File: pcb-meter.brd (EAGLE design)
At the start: 65.5 x 35 mm, 47 parts

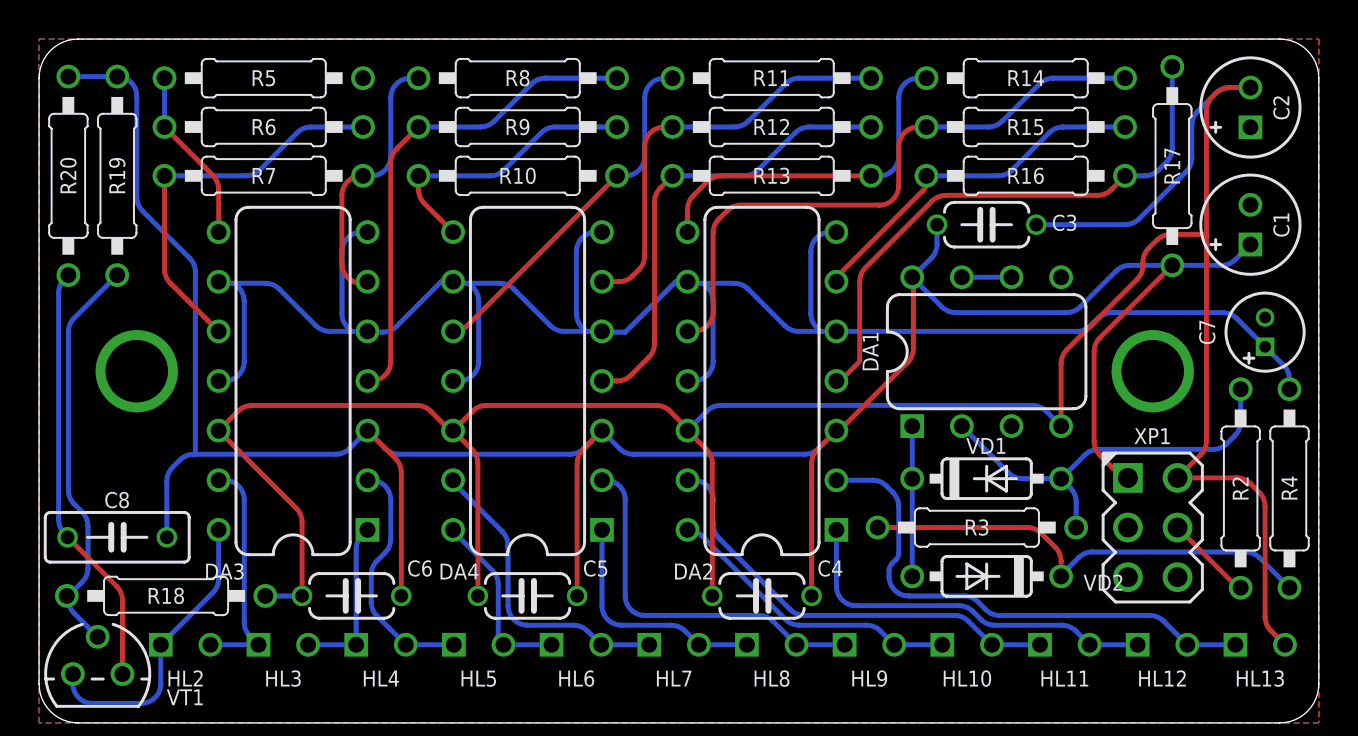
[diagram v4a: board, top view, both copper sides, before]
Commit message: Add Meter Board
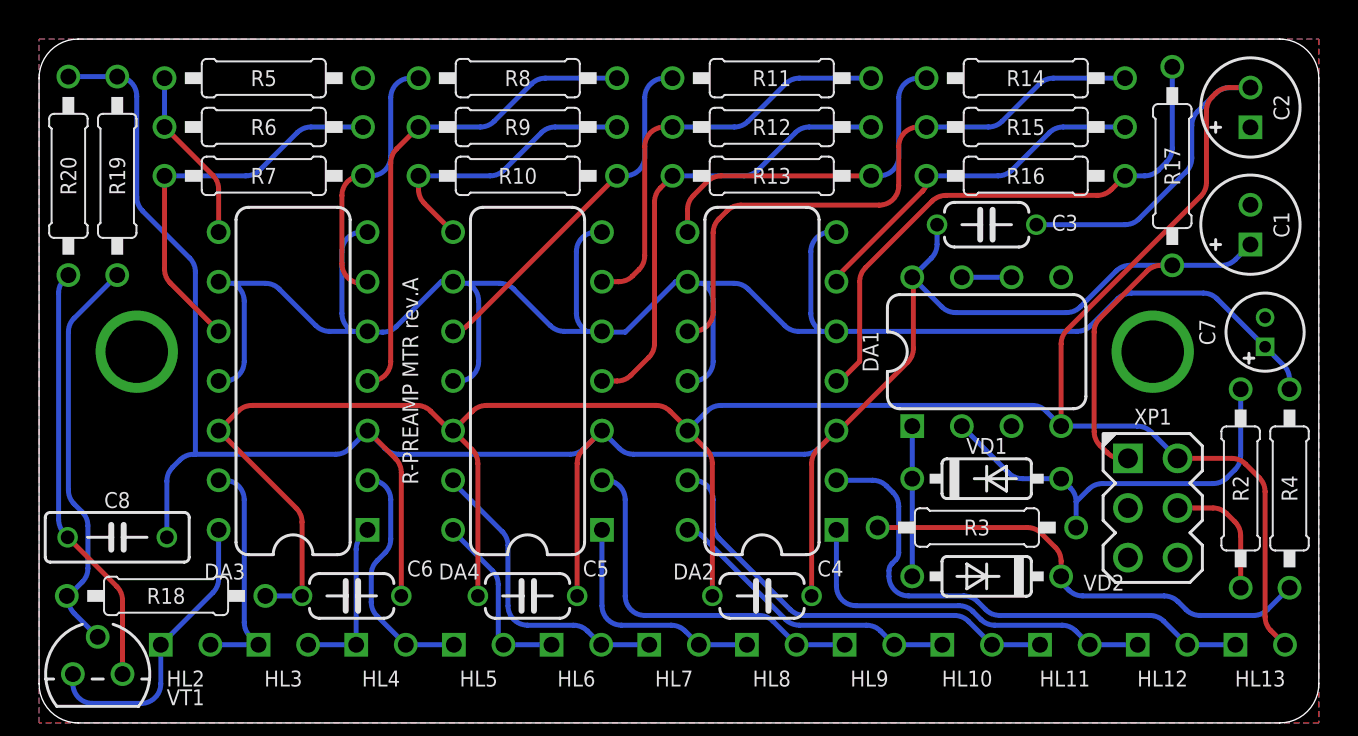
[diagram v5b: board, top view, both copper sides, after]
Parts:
- added PCB1: R-PREAMP MTR rev.A, module-footprints:F-LOGO
- C1, C2: value 10u/35V -> 10U/35V
- C3, C4, C5, C6: value 100n -> 100N(TH)
- C7: value 1u/50V -> 1U/50V
- C8: value 47n -> 47N(FILM)
- R10: value 560R -> 560R(TH)
- R11: value 820R -> 820R(TH)
- R12: value 1.2k -> 1K2(TH)
- R13: value 1.5k -> 1K5(TH)
- R14: value 2.2k -> 2K2(TH)
- R15: value 3.3k -> 3K3(TH)
- R16: value 12k -> 12K(TH)
- R17: value 5.6k -> 5K6(TH)
- R18: value 15k -> 15K(TH)
- R19: value 1k -> 1K(TH)
- R2: value 56k -> 56K(TH)
- R20: value 180R -> 180R(TH)
- R3: value 150k -> 150K(TH)
- R4: value 1.8k -> 1K8(TH)
- R5: value 270R -> 270R(TH)
- R6, R7: value 220R -> 220R(TH)
- R8, R9: value 330R -> 330R(TH)
- moved XP1 1.00 mm to (90.0, 13.0)
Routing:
- net -15V: track 139.7 -> 132.9 mm
- net N$2: track 4.51 -> 6.60 mm
- net N$26: track 97.5 -> 98.3 mm
- net N$5: track 21.0 -> 21.7 mm

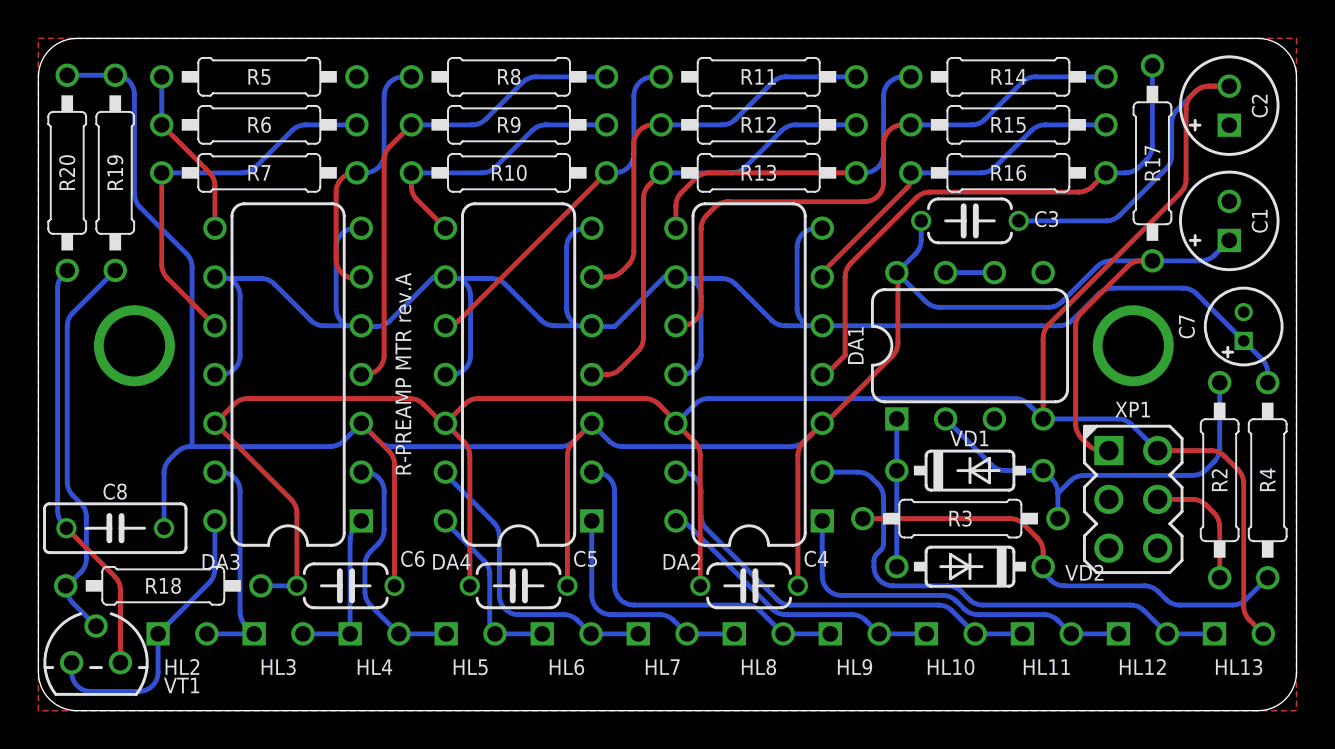
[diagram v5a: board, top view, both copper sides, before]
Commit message: Change meter PCB size
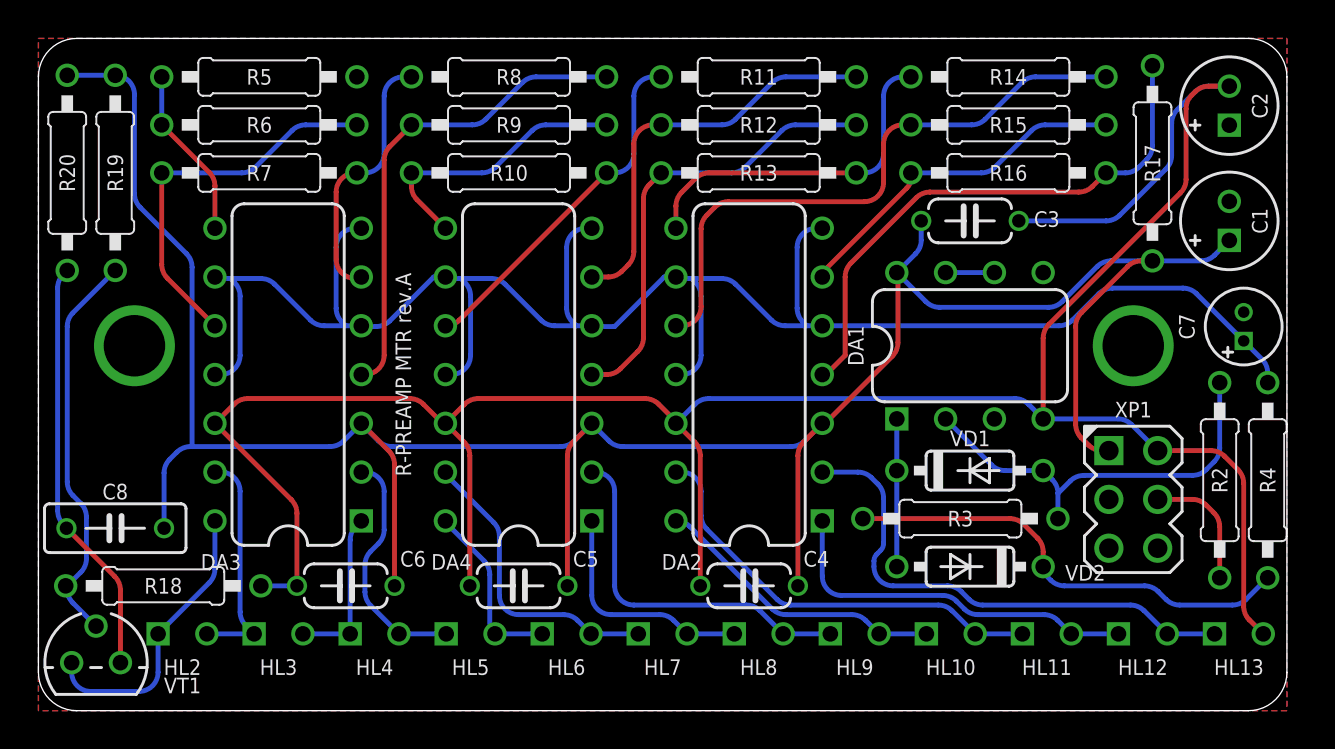
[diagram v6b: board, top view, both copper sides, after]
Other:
- board size 65.5 x 35 mm -> 65 x 35 mm
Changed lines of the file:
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@@
 <wire x1="33" y1="35" x2="33" y2="4" width="0" layer="20"/>
 <wire x1="33" y1="4" x2="35" y2="2" width="0" layer="20" curve="90"/>
-<wire x1="35" y1="2" x2="96.5" y2="2" width="0" layer="20"/>
-<wire x1="96.5" y1="2" x2="98.5" y2="4" width="0" layer="20" curve="90"/>
-<wire x1="98.5" y1="4" x2="98.5" y2="35" width="0" layer="20"/>
-<wire x1="98.5" y1="35" x2="96.5" y2="37" width="0" layer="20" curve="90"/>
-<wire x1="96.5" y1="37" x2="35" y2="37" width="0" layer="20"/>
+<wire x1="35" y1="2" x2="96" y2="2" width="0" layer="20"/>
+<wire x1="96" y1="2" x2="98" y2="4" width="0" layer="20" curve="90"/>
+<wire x1="98" y1="4" x2="98" y2="35" width="0" layer="20"/>
+<wire x1="98" y1="35" x2="96" y2="37" width="0" layer="20" curve="90"/>
+<wire x1="96" y1="37" x2="35" y2="37" width="0" layer="20"/>
 <wire x1="35" y1="37" x2="33" y2="35" width="0" layer="20" curve="90"/>
 </plain>
@@
 <polygon width="0.254" layer="16">
 <vertex x="33" y="37"/>
-<vertex x="98.5" y="37"/>
-<vertex x="98.5" y="2"/>
+<vertex x="98" y="37"/>
+<vertex x="98" y="2"/>
 <vertex x="33" y="2"/>
 </polygon>
 <polygon width="0.254" layer="1">
 <vertex x="33" y="37"/>
-<vertex x="98.5" y="37"/>
-<vertex x="98.5" y="2"/>
+<vertex x="98" y="37"/>
+<vertex x="98" y="2"/>
 <vertex x="33" y="2"/>
 </polygon>

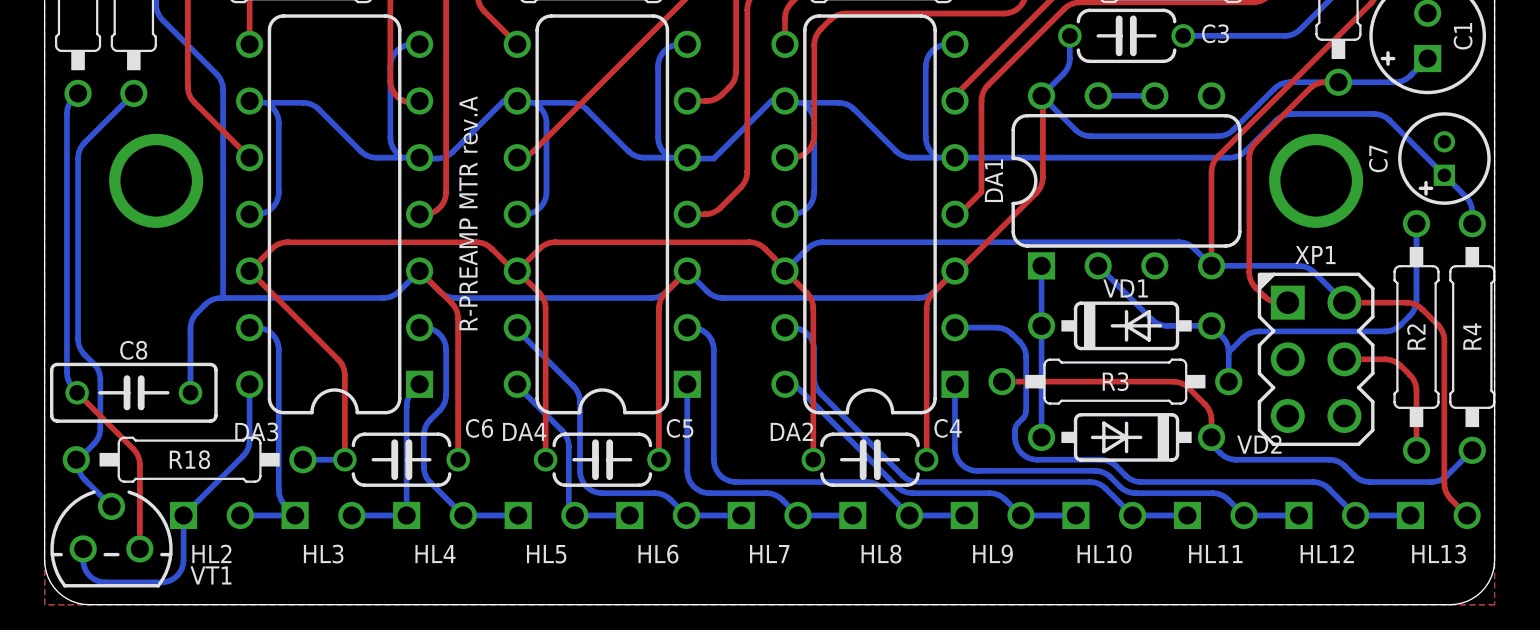
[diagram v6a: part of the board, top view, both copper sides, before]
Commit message: Change LED/front panel spacing
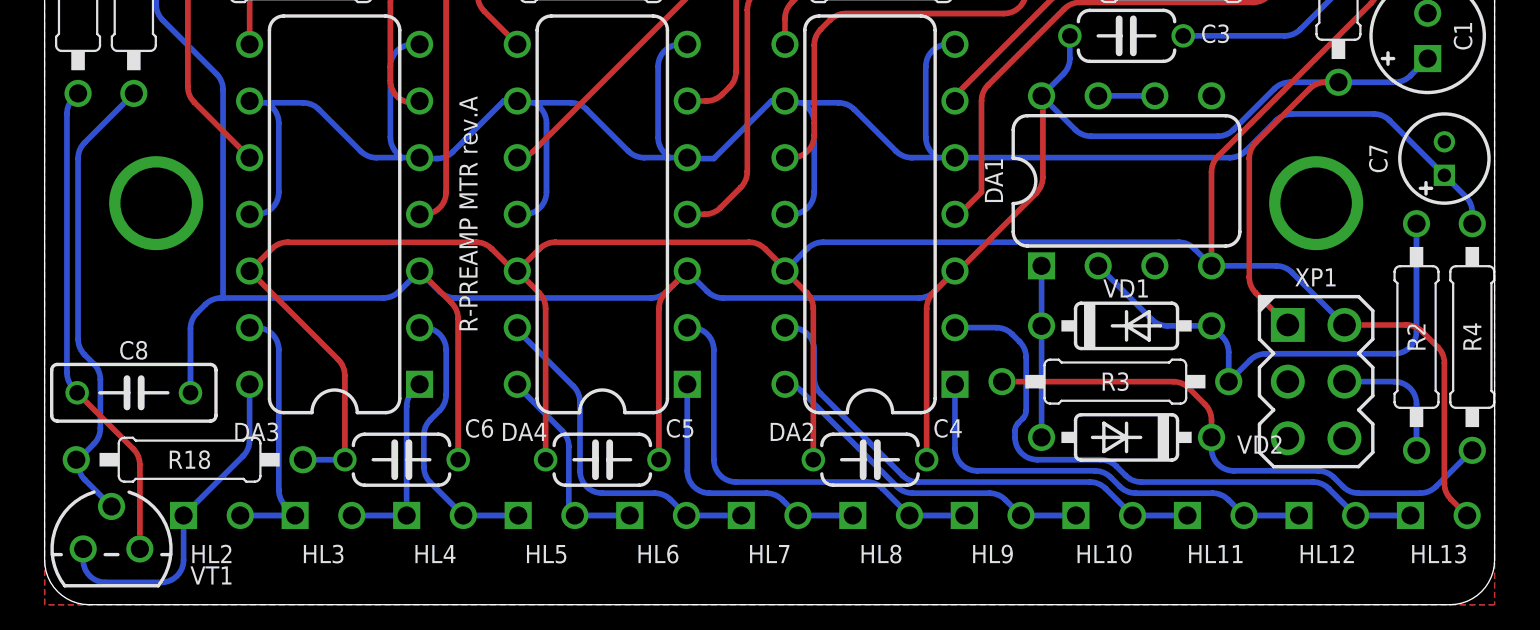
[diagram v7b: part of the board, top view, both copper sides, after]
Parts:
- moved XP1 1.00 mm to (90.0, 12.0)
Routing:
- net N$5: track 21.7 -> 23.0 mm
- net N$2: track 6.60 -> 5.72 mm
- net +15V: track 135.3 -> 136.0 mm
- net N$8: track 24.0 -> 24.6 mm
- net -15V: track 132.9 -> 132.3 mm
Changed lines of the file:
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@@
 </autorouter>
 <elements>
-<element name="XP1" library="connectors" package="MA03-2" value="" x="90" y="13" rot="R270"/>
+<element name="XP1" library="connectors" package="MA03-2" value="" x="90" y="12" rot="R270"/>
 <element name="R2" library="resistors" package="R-0207/10" value="56K(TH)" x="94.5" y="14" rot="R90"/>
 <element name="DA1" library="ic-ti" package="DIP-8" value="TL072IP" x="81.5" y="21">
@@
 <wire x1="92.45710625" y1="28.95710625" x2="85.60289375" y2="22.10289375" width="0.254" layer="1"/>
 <wire x1="85.60289375" y1="22.10289375" x2="85.31" y2="21.3957875" width="0.254" layer="1" curve="45"/>
-<wire x1="91.27" y1="15.54" x2="94.0457875" y2="15.54" width="0.254" layer="1"/>
-<wire x1="94.0457875" y1="15.54" x2="94.75289375" y2="15.24710625" width="0.254" layer="1" curve="-45"/>
-<wire x1="94.75289375" y1="15.24710625" x2="95.45710625" y2="14.54289375" width="0.254" layer="1"/>
-<wire x1="95.45710625" y1="14.54289375" x2="95.75" y2="13.8357875" width="0.254" layer="1" curve="-45"/>
-<wire x1="95.75" y1="13.8357875" x2="95.75" y2="7.4342125" width="0.254" layer="1"/>
+<wire x1="92.75" y1="33.3357875" x2="92.75" y2="29.6642125" width="0.254" layer="1"/>
+<wire x1="92.75" y1="29.6642125" x2="92.45710625" y2="28.95710625" width="0.254" layer="1" curve="-45"/>
+<wire x1="85.31" y1="17.19" x2="88.2057875" y2="17.19" width="0.254" layer="16"/>
+<wire x1="88.2057875" y1="17.19" x2="88.91289375" y2="16.89710625" width="0.254" layer="16" curve="-45"/>
+<wire x1="88.91289375" y1="16.89710625" x2="91.27" y2="14.54" width="0.254" layer="16"/>
+<wire x1="91.27" y1="14.54" x2="94.0457875" y2="14.54" width="0.254" layer="1"/>
+<wire x1="94.0457875" y1="14.54" x2="94.75289375" y2="14.24710625" width="0.254" layer="1" curve="-45"/>
+<wire x1="94.75289375" y1="14.24710625" x2="95.45710625" y2="13.54289375" width="0.254" layer="1"/>
+<wire x1="95.45710625" y1="13.54289375" x2="95.75" y2="12.8357875" width="0.254" layer="1" curve="-45"/>
+<wire x1="95.75" y1="12.8357875" x2="95.75" y2="7.4342125" width="0.254" layer="1"/>
 <wire x1="95.75" y1="7.4342125" x2="96.04289375" y2="6.72710625" width="0.254" layer="1" curve="45"/>
 <wire x1="96.04289375" y1="6.72710625" x2="96.77" y2="6" width="0.254" layer="1"/>
-<wire x1="85.31" y1="17.19" x2="89.2057875" y2="17.19" width="0.254" layer="16"/>
-<wire x1="89.2057875" y1="17.19" x2="89.91289375" y2="16.89710625" width="0.254" layer="16" curve="-45"/>
-<wire x1="89.91289375" y1="16.89710625" x2="91.27" y2="15.54" width="0.254" layer="16"/>
-<wire x1="92.75" y1="33.3357875" x2="92.75" y2="29.6642125" width="0.254" layer="1"/>
-<wire x1="92.75" y1="29.6642125" x2="92.45710625" y2="28.95710625" width="0.254" layer="1" curve="-45"/>
 </signal>
 <signal name="+15V">
@@
 <wire x1="77.75" y1="21.1642125" x2="77.75" y2="24.75" width="0.254" layer="1"/>
 <wire x1="77.75" y1="24.75" x2="77.69" y2="24.81" width="0.254" layer="1"/>
-<wire x1="88.73" y1="15.54" x2="88.3742125" y2="15.54" width="0.254" layer="1"/>
-<wire x1="88.3742125" y1="15.54" x2="87.66710625" y2="15.83289375" width="0.254" layer="1" curve="-45"/>
-<wire x1="87.66710625" y1="15.83289375" x2="87.29289375" y2="16.20710625" width="0.254" layer="1"/>
-<wire x1="87.29289375" y1="16.20710625" x2="87" y2="16.9142125" width="0.254" layer="1" curve="-45"/>
-<wire x1="87" y1="16.9142125" x2="87" y2="22.0057875" width="0.254" layer="1"/>
+<wire x1="87" y1="22.0057875" x2="87" y2="16.6842125" width="0.254" layer="1"/>
+<wire x1="87" y1="16.6842125" x2="87.29289375" y2="15.97710625" width="0.254" layer="1" curve="45"/>
+<wire x1="87.29289375" y1="15.97710625" x2="88.73" y2="14.54" width="0.254" layer="1"/>
 <wire x1="87" y1="22.0057875" x2="87.29289375" y2="22.71289375" width="0.254" layer="1" curve="-45"/>
 <wire x1="87.29289375" y1="22.71289375" x2="89.70710625" y2="25.12710625" width="0.254" layer="1"/>
@@
 <contactref element="XP1" pad="4"/>
 <contactref element="R2" pad="1"/>
-<wire x1="91.27" y1="13" x2="93.0857875" y2="13" width="0.254" layer="1"/>
-<wire x1="93.0857875" y1="13" x2="93.79289375" y2="12.70710625" width="0.254" layer="1" curve="-45"/>
-<wire x1="93.79289375" y1="12.70710625" x2="94.20710625" y2="12.29289375" width="0.254" layer="1"/>
-<wire x1="94.20710625" y1="12.29289375" x2="94.5" y2="11.5857875" width="0.254" layer="1" curve="-45"/>
-<wire x1="94.5" y1="11.5857875" x2="94.5" y2="8.92" width="0.254" layer="1"/>
+<wire x1="91.27" y1="12" x2="93.5" y2="12" width="0.254" layer="16"/>
+<wire x1="93.5" y1="12" x2="94.5" y2="11" width="0.254" layer="16" curve="-90"/>
+<wire x1="94.5" y1="11" x2="94.5" y2="8.92" width="0.254" layer="16"/>
 </signal>
 <signal name="N$3">
-<via x="90" y="21" extent="1-16" drill="3.2"/>
+<via x="90" y="20" extent="1-16" drill="3.2"/>
 </signal>
 <signal name="N$4">
-<via x="38" y="21" extent="1-16" drill="3.2"/>
+<via x="38" y="20" extent="1-16" drill="3.2"/>
 </signal>
 <signal name="N$5">
@@
 <wire x1="86.08" y1="13.3157875" x2="85.78710625" y2="14.02289375" width="0.254" layer="16" curve="45"/>
 <wire x1="85.78710625" y1="14.02289375" x2="85.31" y2="14.5" width="0.254" layer="16"/>
-<wire x1="94.5" y1="19.08" x2="94.5" y2="15.6642125" width="0.254" layer="16"/>
-<wire x1="94.5" y1="15.6642125" x2="94.20710625" y2="14.95710625" width="0.254" layer="16" curve="-45"/>
-<wire x1="94.20710625" y1="14.95710625" x2="93.79289375" y2="14.54289375" width="0.254" layer="16"/>
-<wire x1="93.79289375" y1="14.54289375" x2="93.0857875" y2="14.25" width="0.254" layer="16" curve="-45"/>
-<wire x1="93.0857875" y1="14.25" x2="87.428425" y2="14.25" width="0.254" layer="16"/>
-<wire x1="87.428425" y1="14.25" x2="86.72131875" y2="13.95710625" width="0.254" layer="16" curve="45"/>
-<wire x1="86.72131875" y1="13.95710625" x2="86.08" y2="13.3157875" width="0.254" layer="16"/>
+<wire x1="94.5" y1="19.08" x2="94.5" y2="14.25" width="0.254" layer="16"/>
+<wire x1="94.5" y1="14.25" x2="93.5" y2="13.25" width="0.254" layer="16" curve="-90"/>
+<wire x1="93.5" y1="13.25" x2="87.7442125" y2="13.25" width="0.254" layer="16"/>
+<wire x1="87.7442125" y1="13.25" x2="87.03710625" y2="12.95710625" width="0.254" layer="16" curve="45"/>
+<wire x1="87.03710625" y1="12.95710625" x2="86.08" y2="12" width="0.254" layer="16"/>
 </signal>
 <signal name="N$7">
@@
 <wire x1="84.29289375" y1="11.70710625" x2="83.5857875" y2="12" width="0.254" layer="1" curve="45"/>
 <wire x1="83.5857875" y1="12" x2="75.92" y2="12" width="0.254" layer="1"/>
-<wire x1="85.31" y1="9.5" x2="85.31" y2="9.19" width="0.254" layer="16"/>
-<wire x1="85.31" y1="9.19" x2="85.70710625" y2="8.79289375" width="0.254" layer="16"/>
-<wire x1="85.70710625" y1="8.79289375" x2="86.4142125" y2="8.5" width="0.254" layer="16" curve="45"/>
-<wire x1="86.4142125" y1="8.5" x2="90.5857875" y2="8.5" width="0.254" layer="16"/>
-<wire x1="90.5857875" y1="8.5" x2="91.29289375" y2="8.20710625" width="0.254" layer="16" curve="-45"/>
-<wire x1="91.29289375" y1="8.20710625" x2="91.70710625" y2="7.79289375" width="0.254" layer="16"/>
-<wire x1="91.70710625" y1="7.79289375" x2="92.4142125" y2="7.5" width="0.254" layer="16" curve="45"/>
-<wire x1="92.4142125" y1="7.5" x2="95.1657875" y2="7.5" width="0.254" layer="16"/>
-<wire x1="95.1657875" y1="7.5" x2="95.87289375" y2="7.79289375" width="0.254" layer="16" curve="45"/>
-<wire x1="95.87289375" y1="7.79289375" x2="97" y2="8.92" width="0.254" layer="16"/>
+<wire x1="85.31" y1="9.5" x2="85.31" y2="9" width="0.254" layer="16"/>
+<wire x1="85.31" y1="9" x2="86.31" y2="8" width="0.254" layer="16" curve="90"/>
+<wire x1="86.31" y1="8" x2="90.0857875" y2="8" width="0.254" layer="16"/>
+<wire x1="90.0857875" y1="8" x2="90.79289375" y2="7.70710625" width="0.254" layer="16" curve="-45"/>
+<wire x1="90.79289375" y1="7.70710625" x2="91.20710625" y2="7.29289375" width="0.254" layer="16"/>
+<wire x1="91.20710625" y1="7.29289375" x2="91.9142125" y2="7" width="0.254" layer="16" curve="45"/>
+<wire x1="91.9142125" y1="7" x2="94.6657875" y2="7" width="0.254" layer="16"/>
+<wire x1="94.6657875" y1="7" x2="95.37289375" y2="7.29289375" width="0.254" layer="16" curve="45"/>
+<wire x1="95.37289375" y1="7.29289375" x2="97" y2="8.92" width="0.254" layer="16"/>
 </signal>
 <signal name="N$6">
